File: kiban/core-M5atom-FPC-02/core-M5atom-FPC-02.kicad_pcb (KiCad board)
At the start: 2 copper layers, 49 x 40 mm, 19 parts, among them J12 TP_VIN, J13 TP_3V3, J14 TP_PGND, J15 TP_PGND, J16 ESP32-01, J17 ESP32-01, J18 TP_PGND, J3 M5atom-L, J4 M5atomS3-R, J5 3V3, J6 5V, J9 I2C, U1 AE-BNO055

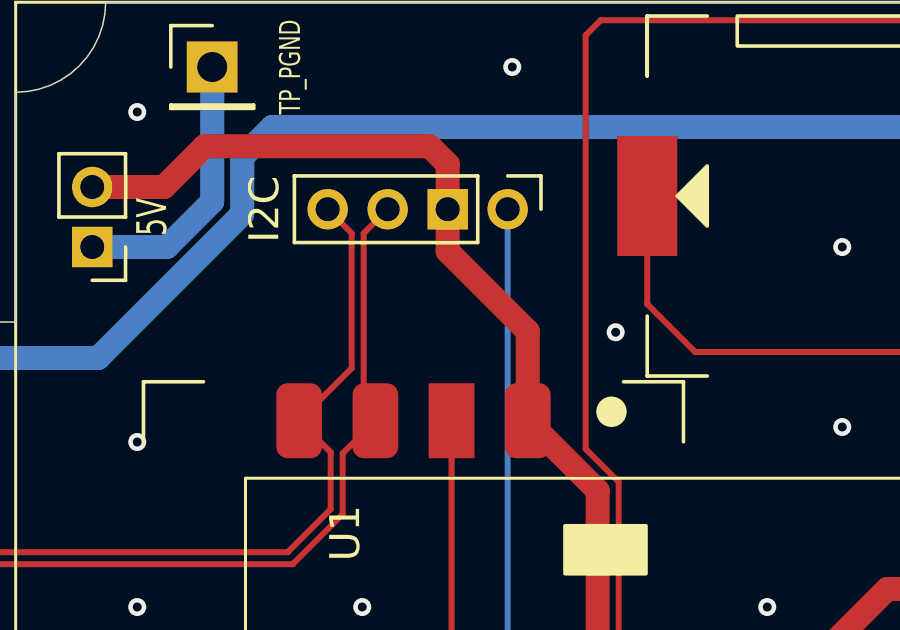
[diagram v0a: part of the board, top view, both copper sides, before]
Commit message: kiban: rename core-M5atom-FPC−02 → core-M5atom-FPC-02 (ASCII hyphen)
Directory and filenames used U+2212 MINUS SIGN instead of ASCII '-',
which rendered as a multi-byte character on GitHub. Pure rename, no
content change.

Co-Authored-By: Claude Opus 5 <noreply@anthropic.com>
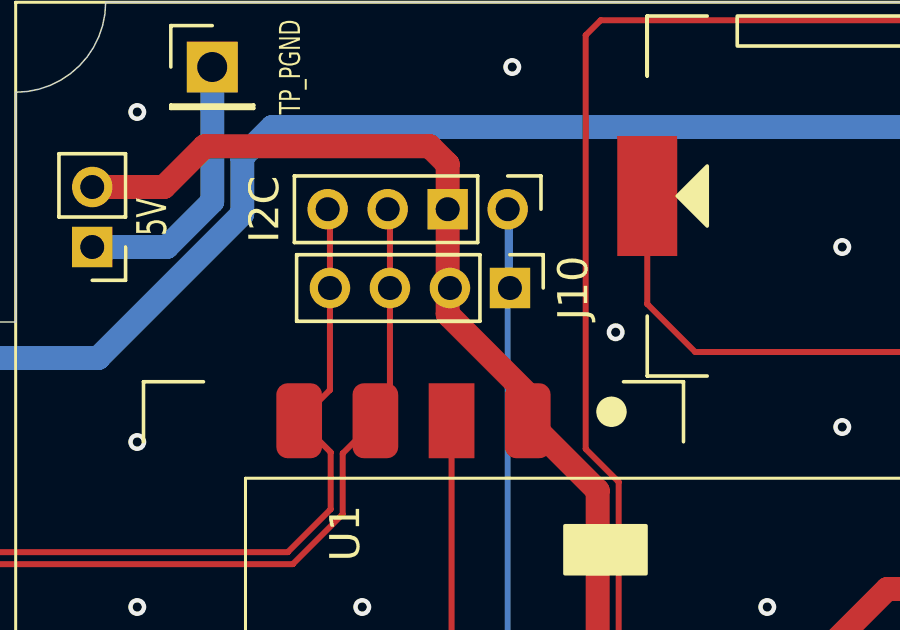
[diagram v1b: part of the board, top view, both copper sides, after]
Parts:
- added J10: I2C, Connector_PinHeader_2.00mm:PinHeader_1x04_P2.00mm_Vertical, F.Cu at (-3.52, -10.5)
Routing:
- net GND: track 122.7 -> 125.4 mm
- net SCL: track 30.7 -> 30.1 mm
